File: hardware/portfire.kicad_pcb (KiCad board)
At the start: 2 copper layers, 176 parts, among them IC101 STM32F4xxVxTx, IC102 TPS62152, IC103 25AA02E48, IC104 ADP3335, IC105 SNx5176B, IC201 MAX5969x, IC202 KSZ8081RNA, IC203 MAX17503, IC301 TPS92512, J201 RJ45, J202 AUX POWER, P101 SWD_TC, P102 AUX_BUS_RX, P103 AUX_BUS_RX, P301 1, P302 2, P303 3, P304 4, P305 5, P306 6, P307 7, P308 8, P309 9, P310 10, P311 11, P312 12, P313 13, P314 14, P315 15, P316 16, P317 17, P318 18, P319 19, P320 20, P321 21, P322 22, P323 23, P324 24, P325 25, P326 26, P327 27, P328 28, P329 29, P330 30, Q301 NTR4501NT1G, Q302 NTR4501NT1G, Q303 NTR4501NT1G, Q304 NTR4501NT1G, Q305 NTR4501NT1G, Q306 NTR4501NT1G, Q307 NTR4501NT1G, Q308 NTR4501NT1G, Q309 NTR4501NT1G, Q310 NTR4501NT1G, Q311 NTR4501NT1G, Q312 NTR4501NT1G, Q313 NTR4501NT1G, Q314 NTR4501NT1G, Q315 NTR4501NT1G, Q316 NTR4501NT1G, Q317 NTR4501NT1G, Q318 NTR4501NT1G, Q319 NTR4501NT1G, Q320 NTR4501NT1G, Q321 NTR4501NT1G, Q322 NTR4501NT1G, Q323 NTR4501NT1G, Q324 NTR4501NT1G, Q325 NTR4501NT1G, Q326 NTR4501NT1G, Q327 NTR4501NT1G, Q328 NTR4501NT1G, Q329 NTR4501NT1G, Q330 NTR4501NT1G, T201 749010012A, Y201 25MHz

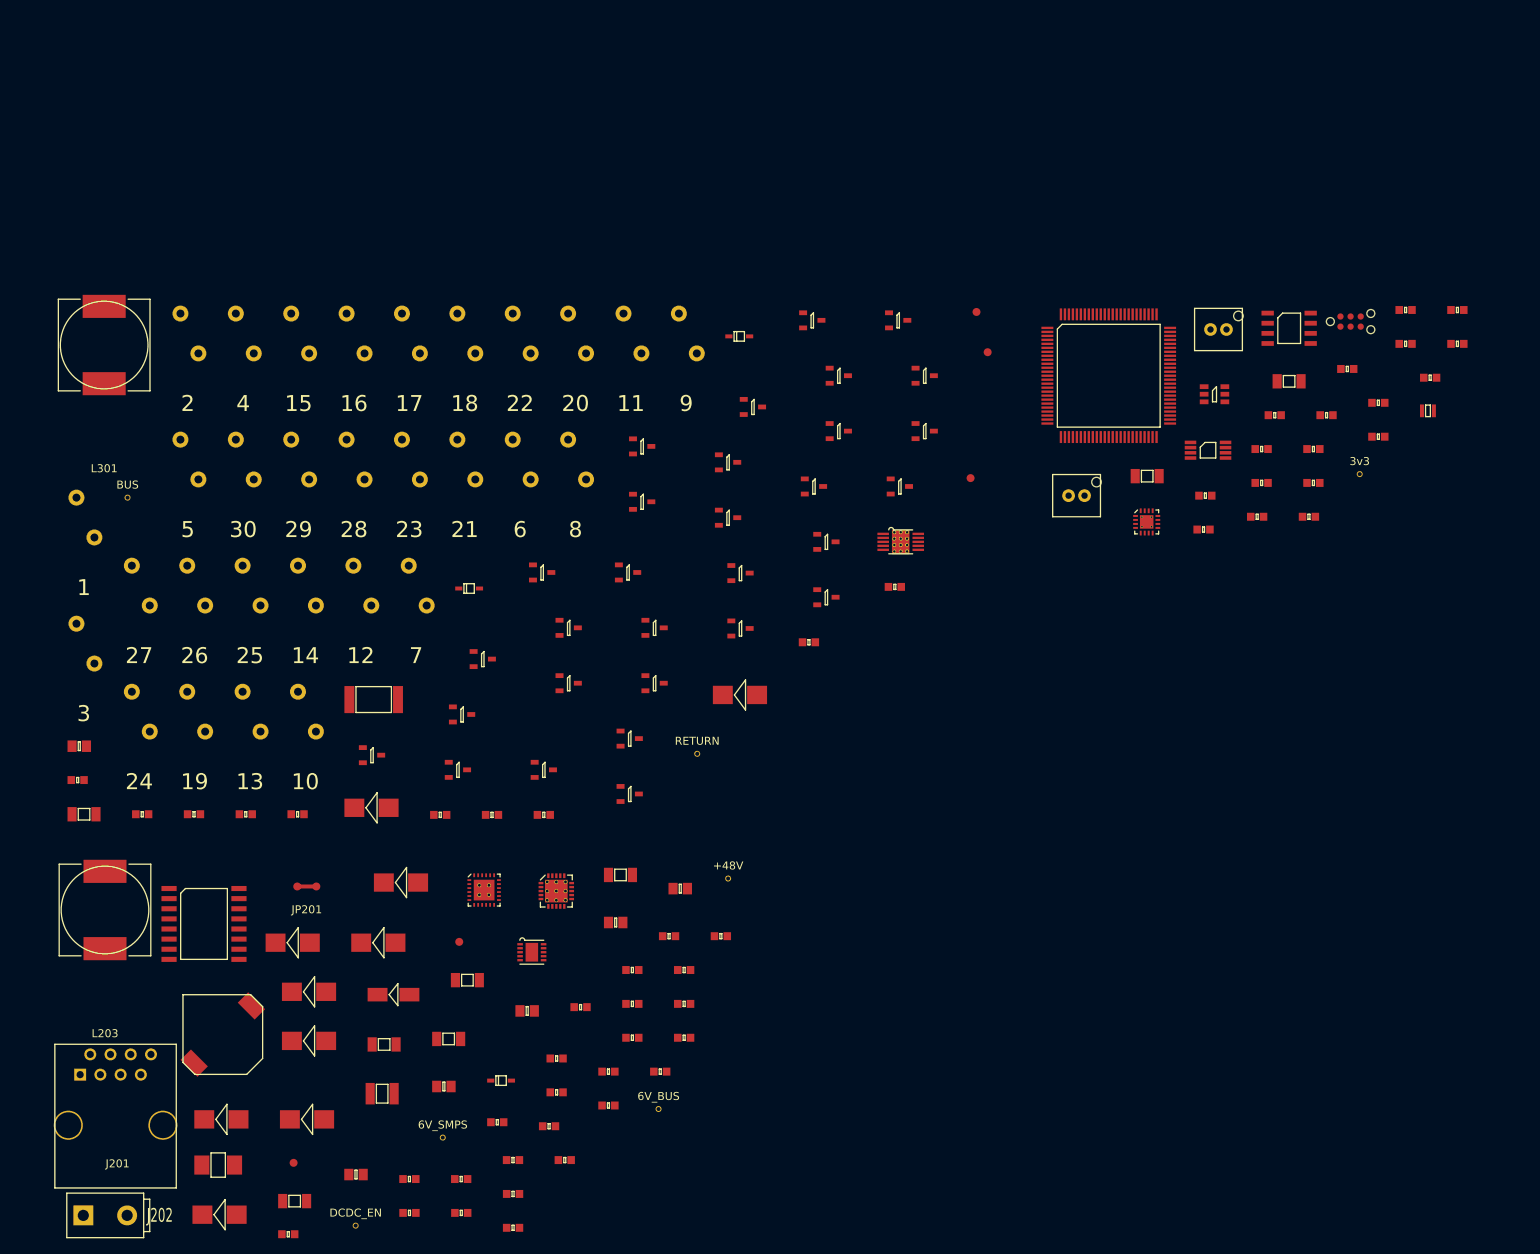
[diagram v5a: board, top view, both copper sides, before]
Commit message: LEDs, ethernet jack
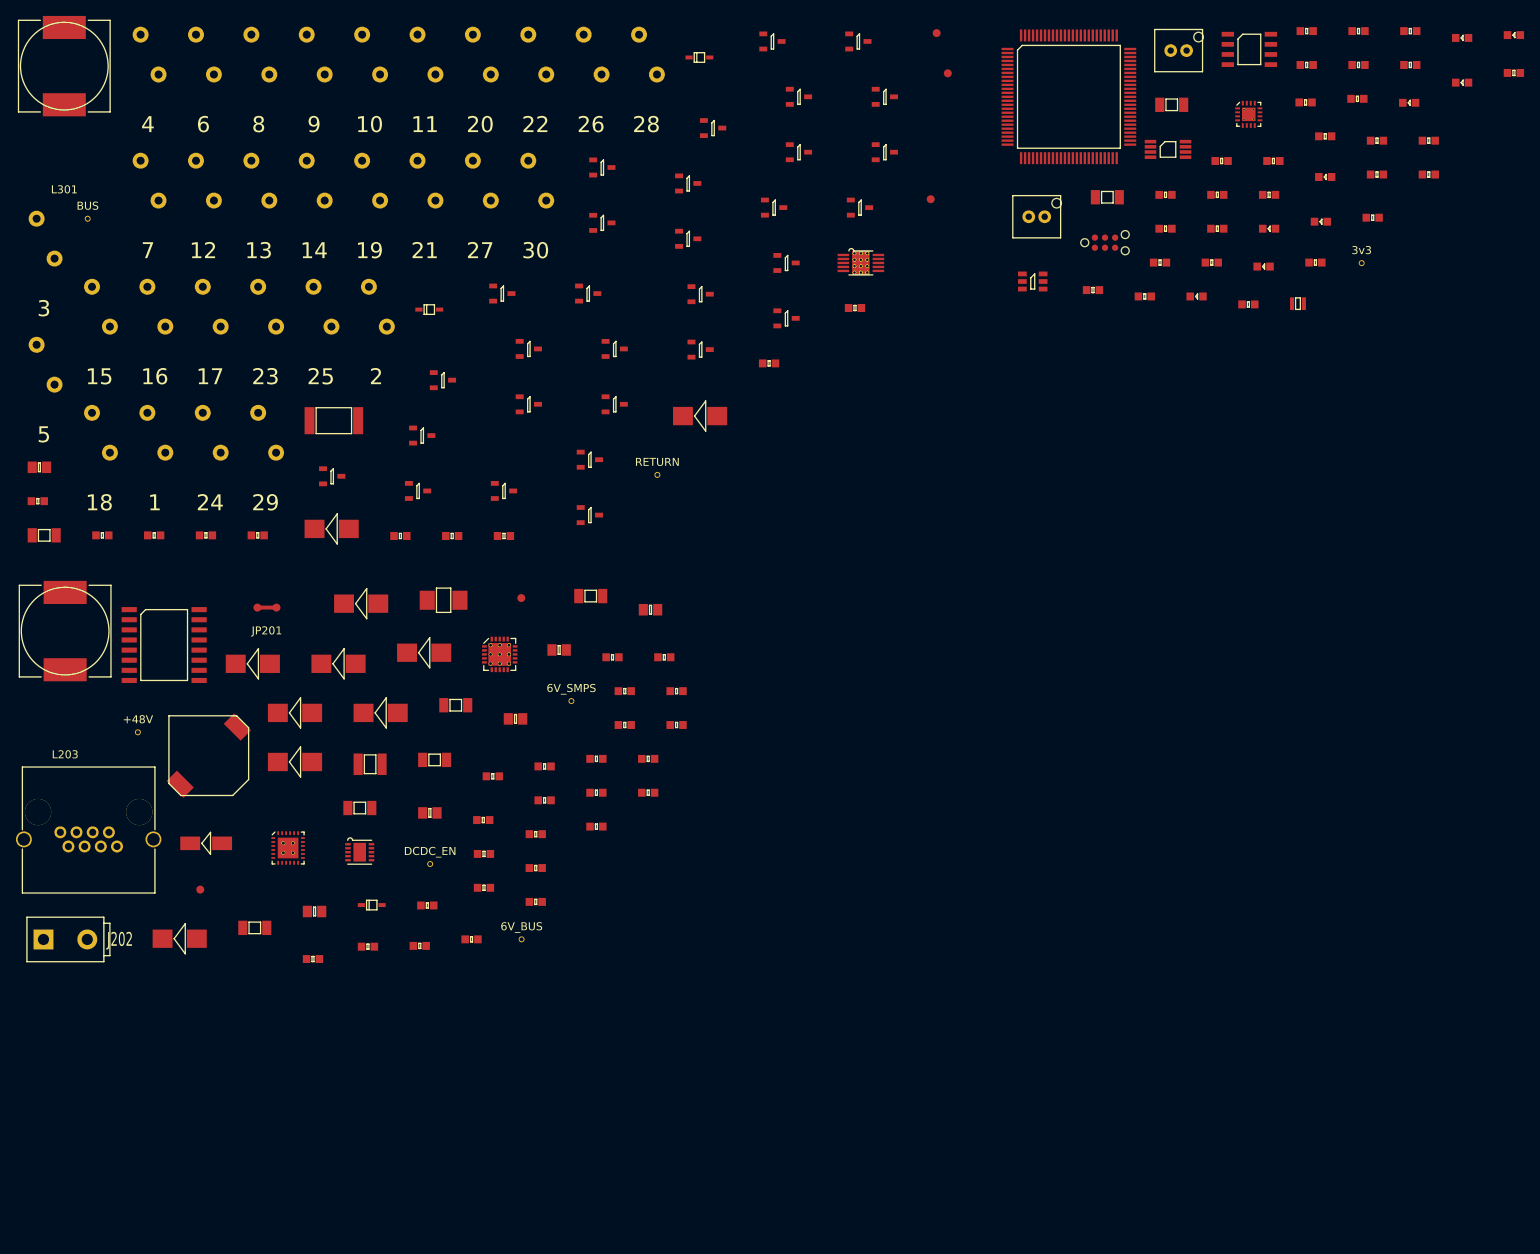
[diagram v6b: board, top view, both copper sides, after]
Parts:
- added C121: 100n, agg:0603, F.Cu at (306.3, 40.9)
- added D101: GREEN, agg:0603-LED, F.Cu at (316.9, 33.6)
- added D102: GREEN, agg:0603-LED, F.Cu at (323.4, 27.6)
- added D103: GREEN, agg:0603-LED, F.Cu at (299.2, 51.0)
- added D104: GREEN, agg:0603-LED, F.Cu at (292.0, 56.7)
- added D105: GREEN, agg:0603-LED, F.Cu at (310.3, 36.1)
- added D106: YELLOW, agg:0603-LED, F.Cu at (316.9, 28.0)
- added D107: RED, agg:0603-LED, F.Cu at (283.6, 60.4)
- added D108: YELLOW, agg:0603-LED, F.Cu at (299.8, 45.4)
- added D109: RED, agg:0603-LED, F.Cu at (292.7, 51.9)
- added R101: 10k, agg:0603, F.Cu at (285.5, 56.2)
- added R102: 1k, agg:0603, F.Cu at (310.4, 31.4)
- added R103: 1k, agg:0603, F.Cu at (310.4, 27.1)
- added R104: 1k, agg:0603, F.Cu at (303.8, 35.6)
- added R105: 1k, agg:0603, F.Cu at (277.1, 60.4)
- added R106: 1k, agg:0603, F.Cu at (299.8, 40.3)
- added R107: 1k, agg:0603, F.Cu at (292.7, 47.7)
- added R108: 1k, agg:0603, F.Cu at (286.2, 51.9)
- added R109: 1k, agg:0603, F.Cu at (279.0, 56.2)
- J201: footprint Connect:RJ45_8 -> hardware:RJHSE5380
- moved R307 99.4 mm to (240.8, 61.9)
- moved Q314 86.7 mm to (222.9, 39.3)
- moved C217 84.5 mm to (207.6, 98.0)
- moved P326 83.2 mm to (207.8, 30.1)
- moved P310 82.9 mm to (180.0, 30.1)
- moved Q316 77.9 mm to (230.4, 28.4)
- moved Y201 76.3 mm to (189.1, 98.6)
- moved TP201 76.3 mm to (150.8, 115.1)
- moved Q307 76.0 mm to (219.8, 53.2)
- moved Q302 75.1 mm to (241.2, 28.4)
- moved D302 72.6 mm to (221.2, 30.4)
- moved C216 70.8 mm to (211.9, 110.0)
- moved P319 70.2 mm to (180.0, 45.9)
- moved R210 66.9 mm to (218.4, 110.0)
- moved P313 66.6 mm to (166.1, 45.9)
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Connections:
- IC101 pad 76: (no net) -> /SWDCLK
- IC103 pad 2: (no net) -> GND
- IC103 pad 6: (no net) -> 3v3
- P101 pad 4: (no net) -> /SWDCLK

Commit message: component grouping on pcb sheet
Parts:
- moved Q302 252.3 mm to (33.0, 171.0)
- moved Q304 231.5 mm to (46.1, 171.1)
- moved Q329 218.7 mm to (31.0, 109.0)
- moved Q330 212.2 mm to (25.0, 109.0)
- moved Q310 207.8 mm to (87.0, 171.0)
- moved Q308 205.1 mm to (74.0, 171.0)
- moved Q328 201.3 mm to (38.1, 110.0)
- moved Q301 201.1 mm to (24.9, 172.0)
- moved C116 195.9 mm to (139.0, 137.0)
- moved Q307 192.9 mm to (67.2, 171.1)
- moved D102 192.0 mm to (178.0, 153.0)
- moved Q303 191.4 mm to (39.1, 170.9)
- moved Q324 191.1 mm to (65.0, 108.0)
- moved P328 191.1 mm to (37.5, 101.5), turned to 180 degrees
- moved P302 189.5 mm to (32.0, 179.0)
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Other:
- board outline added: 100 x 100 mm

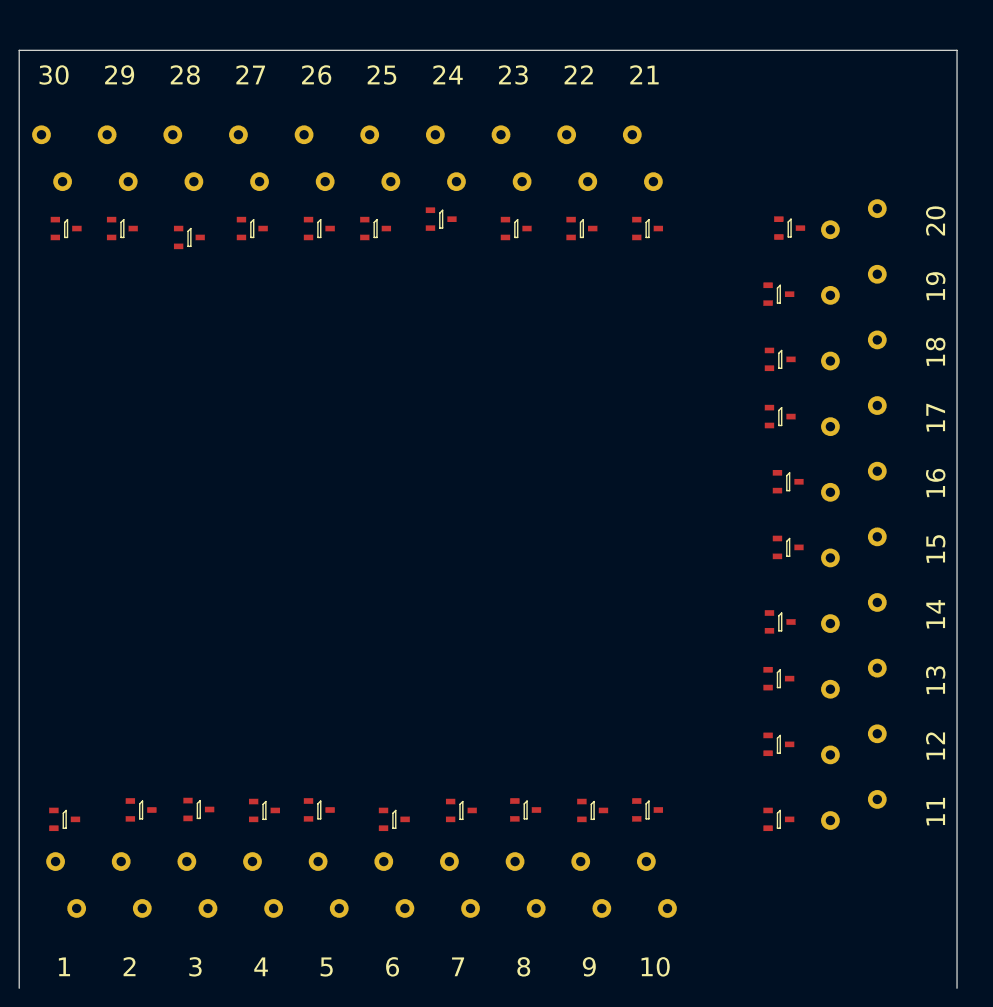
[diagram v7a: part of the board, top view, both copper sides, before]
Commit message: mounting holes
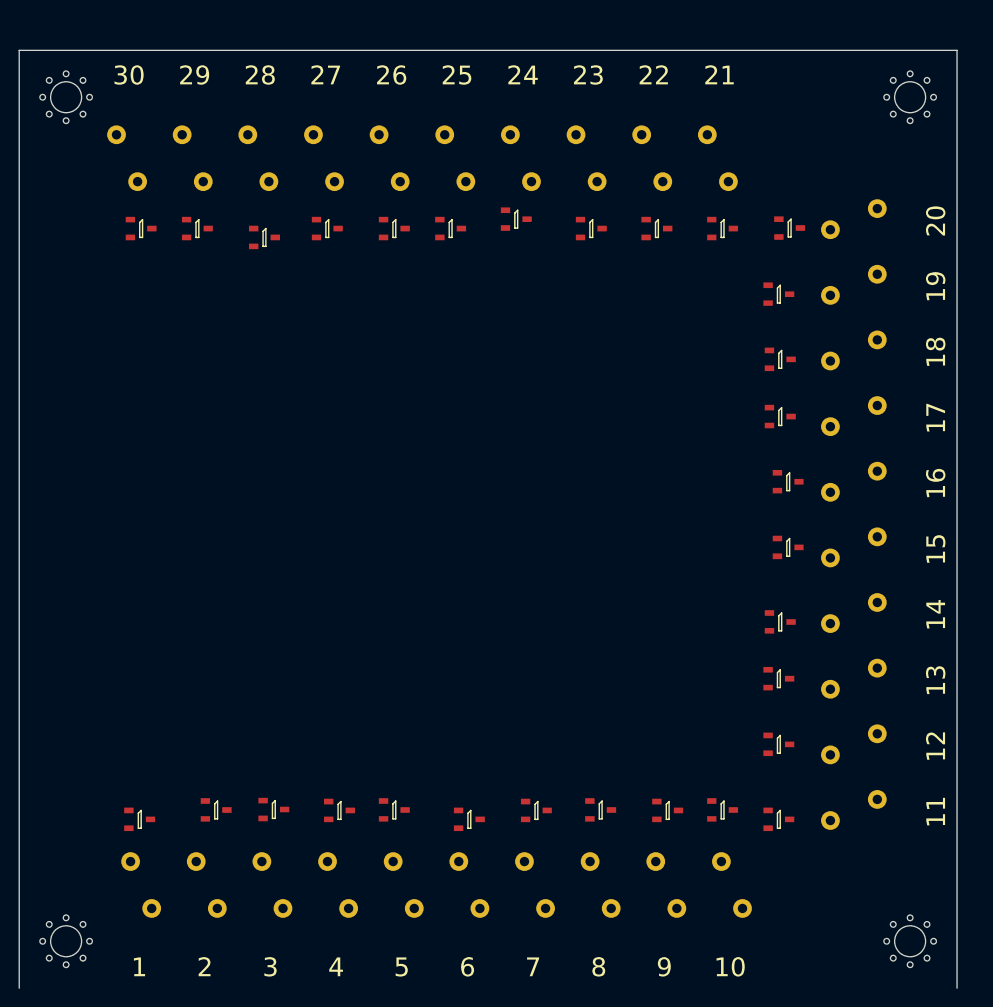
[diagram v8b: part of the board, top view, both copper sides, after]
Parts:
- added X101: PART, agg:M3_MOUNT, F.Cu at (25.0, 95.0)
- added X102: PART, agg:M3_MOUNT, F.Cu at (115.0, 95.0)
- added X103: PART, agg:M3_MOUNT, F.Cu at (115.0, 185.0)
- added X104: PART, agg:M3_MOUNT, F.Cu at (25.0, 185.0)
- moved P301 8.00 mm to (33.0, 179.0)
- moved P302 8.00 mm to (40.0, 179.0)
- moved P303 8.00 mm to (47.0, 179.0)
- moved P304 8.00 mm to (54.0, 179.0)
- moved P305 8.00 mm to (61.0, 179.0)
- moved P306 8.00 mm to (68.0, 179.0)
- moved P307 8.00 mm to (75.0, 179.0)
- moved P308 8.00 mm to (82.0, 179.0)
- moved P309 8.00 mm to (89.0, 179.0)
- moved P310 8.00 mm to (96.0, 179.0)
- moved P321 8.00 mm to (94.5, 101.5)
- moved P322 8.00 mm to (87.5, 101.5)
- moved P323 8.00 mm to (80.5, 101.5)
- moved P324 8.00 mm to (73.5, 101.5)
- moved P325 8.00 mm to (66.5, 101.5)
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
